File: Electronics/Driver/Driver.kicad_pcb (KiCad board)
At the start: 2 copper layers, 70 x 50 mm, 18 parts, among them U1 DRV8428RTER, U2 DB125-2.54-4P-GN, U3 DB125-2.54-4P-GN

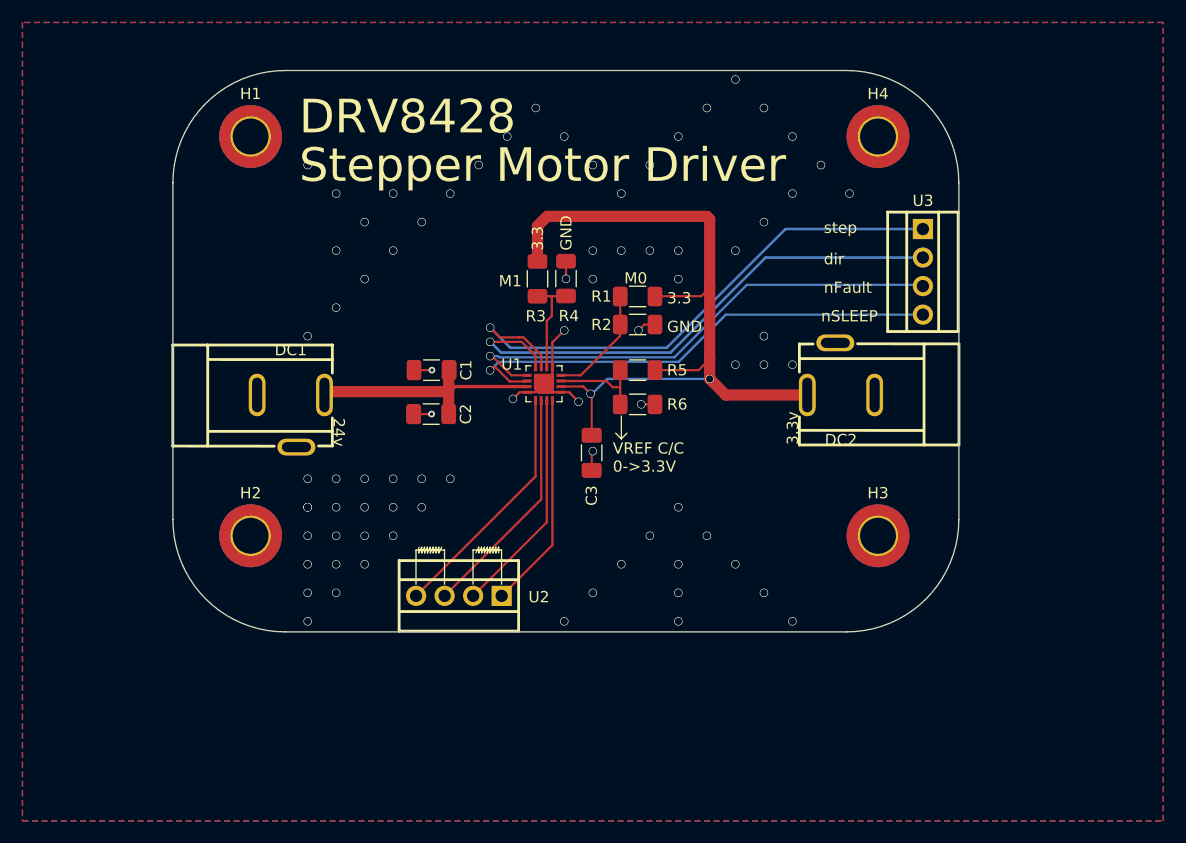
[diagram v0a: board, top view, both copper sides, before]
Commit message: Updated driver PCB
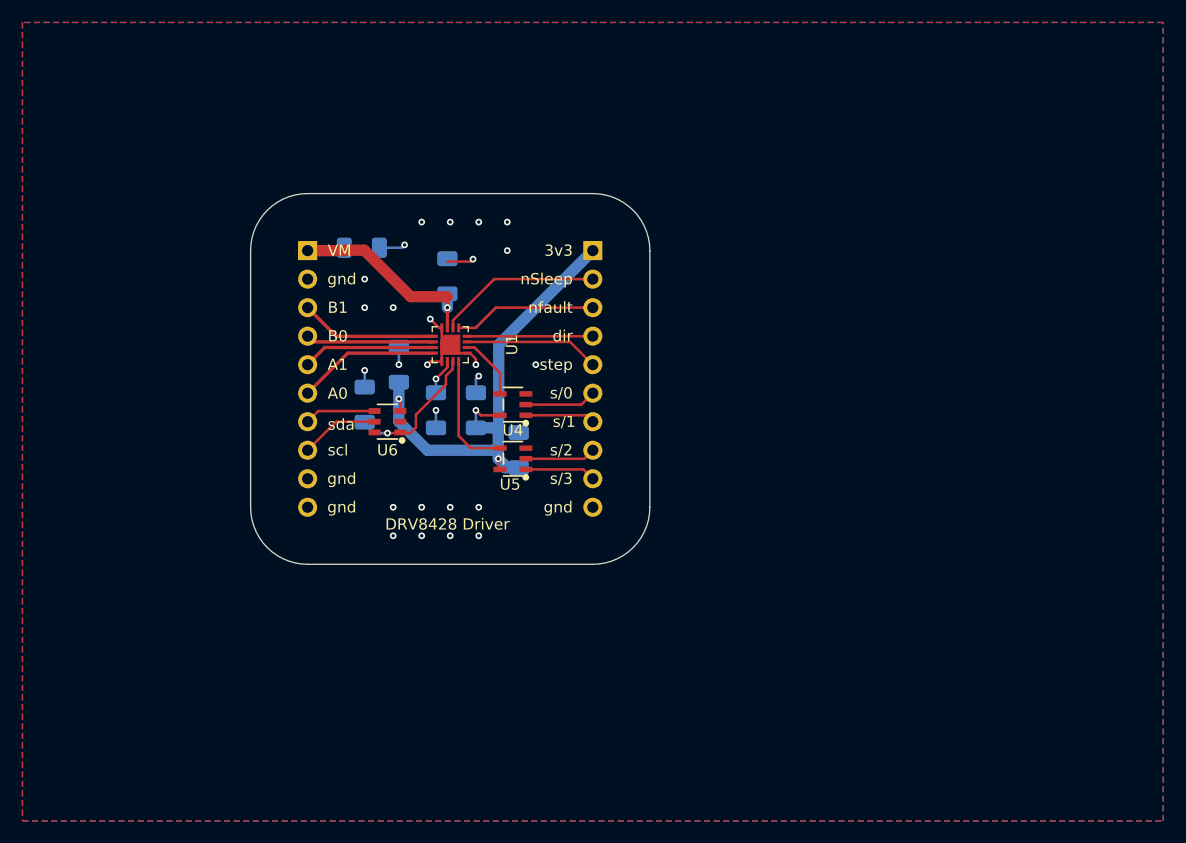
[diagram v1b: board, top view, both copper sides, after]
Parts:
- removed DC1, DC2: DC-005-20A_C136744, COMPONENTS:DC-IN-TH_DC-005-20A
- removed H1, H2, H3, H4: MountingHole_Pad, MountingHole:MountingHole_3.2mm_M3_DIN965_Pad_TopBottom
- removed R1, R2, R3, R4, R5, R6: 0, Resistor_SMD:R_1206_3216Metric_Pad1.30x1.75mm_HandSolder
- removed U2, U3: DB125-2.54-4P-GN, COMPONENTS:CONN-TH_DB125-2.54-4P-GN
- added C4: 0.1u, Capacitor_SMD:C_1206_3216Metric_Pad1.33x1.80mm_HandSolder, B.Cu at (142.0, 80.3)
- added C5: 0.1u, Capacitor_SMD:C_1206_3216Metric_Pad1.33x1.80mm_HandSolder, B.Cu at (145.8, 83.8)
- added C6: 0.1u, Capacitor_SMD:C_1206_3216Metric_Pad1.33x1.80mm_HandSolder, B.Cu at (132.1, 79.8)
- added C7: 0.1u, Capacitor_SMD:C_1206_3216Metric_Pad1.33x1.80mm_HandSolder, B.Cu at (135.1, 76.2)
- added J1: Conn_01x10_Pin, Connector_PinSocket_2.54mm:PinSocket_1x10_P2.54mm_Vertical, B.Cu at (127.0, 66.0)
- added J2: Conn_01x10_Pin, Connector_PinSocket_2.54mm:PinSocket_1x10_P2.54mm_Vertical, B.Cu at (152.4, 66.0)
- added U4: SN74LVC1G125DBVR, COMPONENTS:SOT-23-5_L3.0-W1.7-P0.95-LS2.8-BL, F.Cu at (145.3, 79.8)
- added U5: SN74LVC1G125DBVR, COMPONENTS:SOT-23-5_L3.0-W1.7-P0.95-LS2.8-BL, F.Cu at (145.3, 84.6)
- added U6: MCP4725A0T-E/CH, COMPONENTS:SOT-23-6_L2.9-W1.6-P0.95-LS2.8-BL, F.Cu at (134.1, 81.3)
- C1, C2, C3: moved to B.Cu
- moved C3 14.4 mm to (138.4, 80.3)
- moved C1 12.5 mm to (131.8, 65.8), turned to 180 degrees
- moved C2 12.4 mm to (139.4, 68.3), turned to -90 degrees
- moved U1 9.05 mm to (139.7, 74.4), turned to -90 degrees
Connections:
- net +3.3V renamed Net-(U1-DVDD)
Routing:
- net Net-(U1-DVDD): track 70.8 -> 3.20 mm, vias 2 -> 1
- net +3.3V: track 0.00 -> 49.4 mm, vias 0 -> 3
- net Net-(J2-Pin_5): track 50.3 -> 12.0 mm, vias 1 -> 0
- net Net-(J2-Pin_4): track 48.0 -> 11.2 mm, vias 1 -> 0
- net Net-(J2-Pin_3): track 45.3 -> 12.7 mm, vias 1 -> 0
- net Net-(J2-Pin_2): track 44.5 -> 14.6 mm, vias 1 -> 0
- net Net-(J1-Pin_4): track 21.0 -> 11.4 mm
- net Net-(J1-Pin_3): track 21.8 -> 12.3 mm
- net Net-(J1-Pin_5): track 20.1 -> 11.8 mm
- net /SCL: track 0.00 -> 7.01 mm
- net /SDA: track 0.00 -> 6.86 mm
- net Net-(J1-Pin_6): track 19.3 -> 12.7 mm
- net Net-(J2-Pin_6): track 0.00 -> 6.38 mm
- net Net-(J2-Pin_9): track 0.00 -> 6.30 mm
- net Net-(J2-Pin_8): track 0.00 -> 6.28 mm
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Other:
- board size 70 x 50 mm -> 35.6 x 33 mm
- board text added: "0.01u"
- board text added: "0.1u"
- board text added: "0.47u"
- board text added: "100u"
- board text added: "3v3"
- board text added: "A0"
- board text added: "A1"
- board text added: "B0"
- board text added: "B1"
- board text added: "DRV8428 Driver"
- board text added: "VM"
- board text added: "gnd"
- board text added: "nSleep"
- board text added: "nfault"
- board text added: "s/0"
- board text added: "s/1"
- board text added: "s/2"
- board text added: "s/3"
- board text added: "scl"
- board text added: "sda"
- board text removed: "24v"
- board text removed: "3.3"
- board text removed: "3.3v"
- board text removed: "DRV8428"
- board text removed: "GND"
- board text removed: "M0"
- board text removed: "M1"
- board text removed: "Stepper Motor Driver"
- board text removed: "VREF C/C 0->3.3V"
- board text removed: "nFault"
- board text removed: "nSLEEP"
